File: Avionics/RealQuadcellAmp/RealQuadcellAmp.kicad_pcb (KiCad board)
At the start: 2 copper layers, 115 x 90.5 mm, 73 parts, among them J1 Screw_Terminal_01x02, J2 Conn_01x04_Pin, U1 OPA1642AID, U2 OPA1642AID, U3 OPA1642AID, U4 OPA1642AID

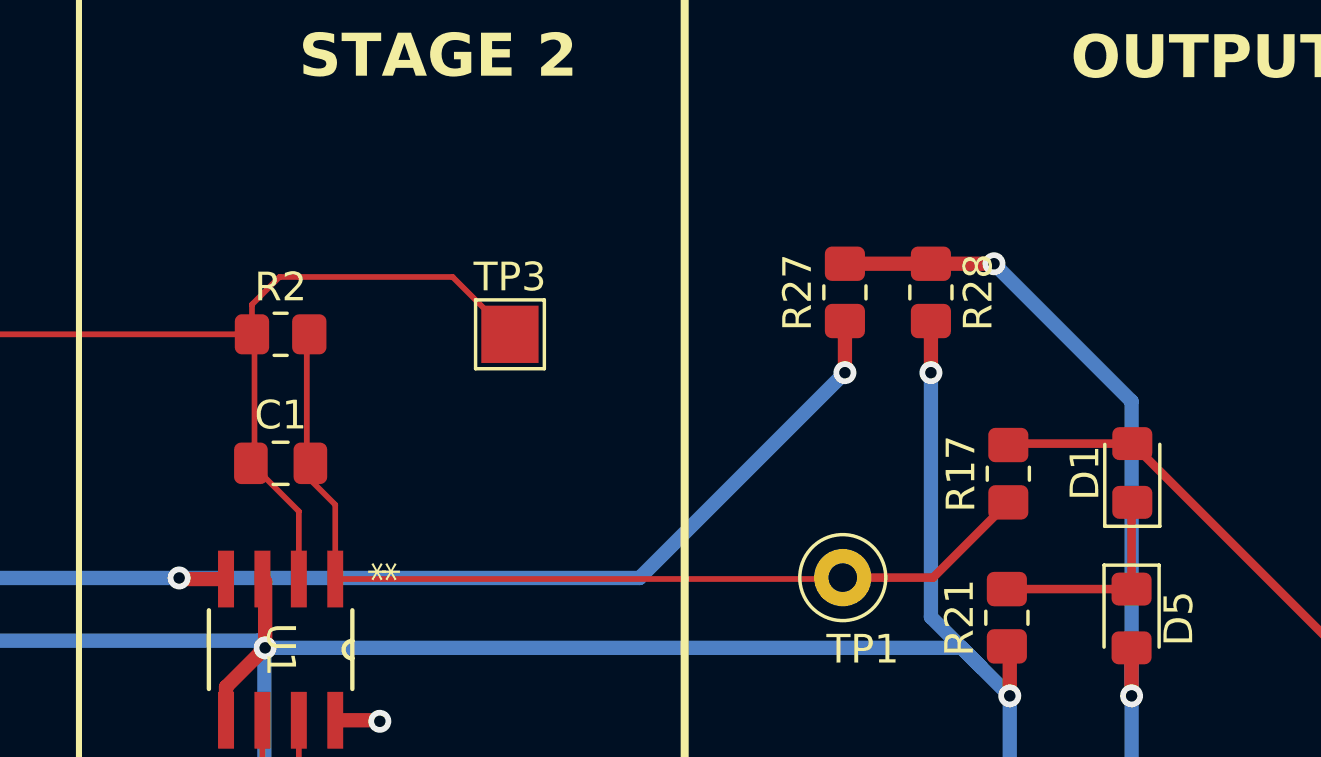
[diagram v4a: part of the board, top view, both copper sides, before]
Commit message: added voltage regulator
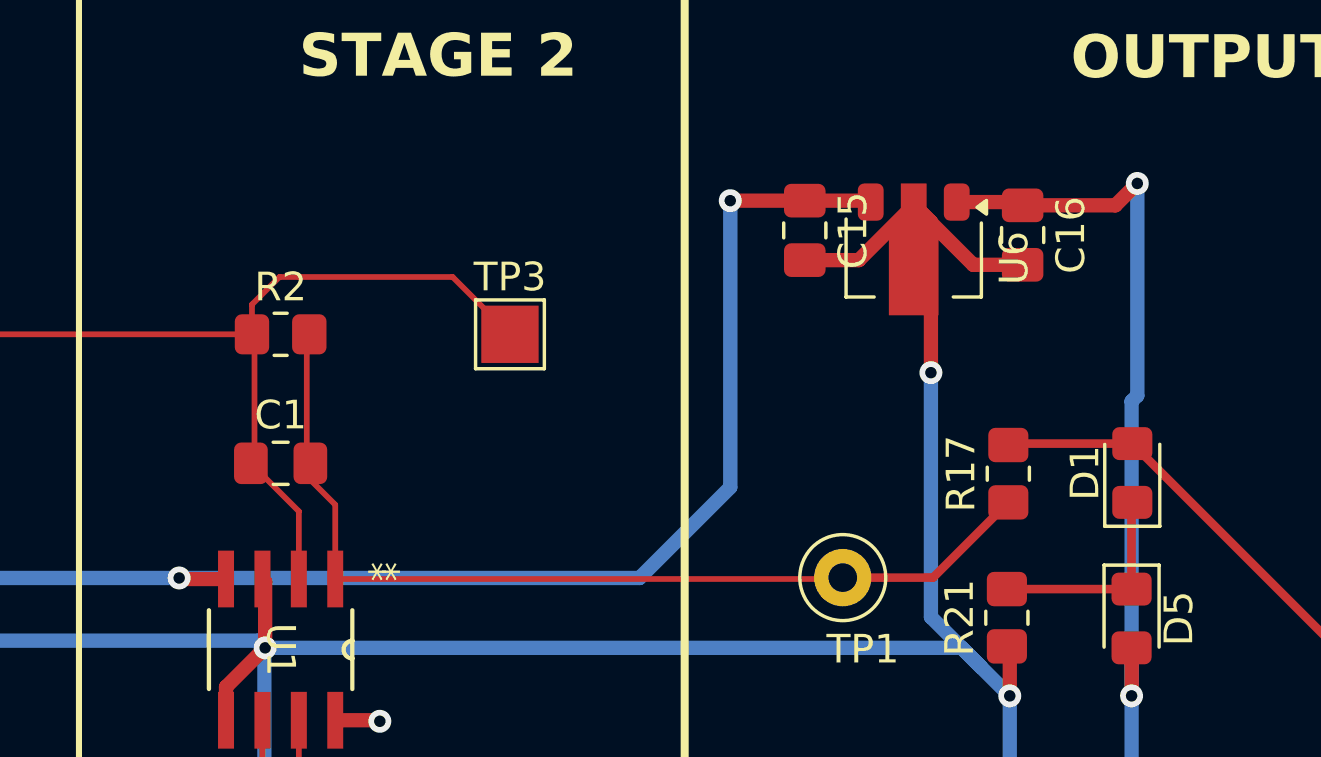
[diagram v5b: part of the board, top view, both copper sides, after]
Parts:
- removed R27: 11k, Resistor_SMD:R_0805_2012Metric_Pad1.20x1.40mm_HandSolder
- removed R28: 29k, Resistor_SMD:R_0805_2012Metric_Pad1.20x1.40mm_HandSolder
- added C15: 0.33u, Capacitor_SMD:C_0805_2012Metric_Pad1.18x1.45mm_HandSolder, F.Cu at (171.6, 49.4)
- added C16: 0.1u, Capacitor_SMD:C_0805_2012Metric_Pad1.18x1.45mm_HandSolder, F.Cu at (179.2, 49.6)
- added U6: L78L33_SOT89, Package_TO_SOT_SMD:SOT-89-3, F.Cu at (175.4, 50.4)
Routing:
- net QUAD_GND: track 308.6 -> 322.2 mm
- net VCC: track 181.0 -> 188.5 mm
- net +3V3: track 75.9 -> 78.2 mm

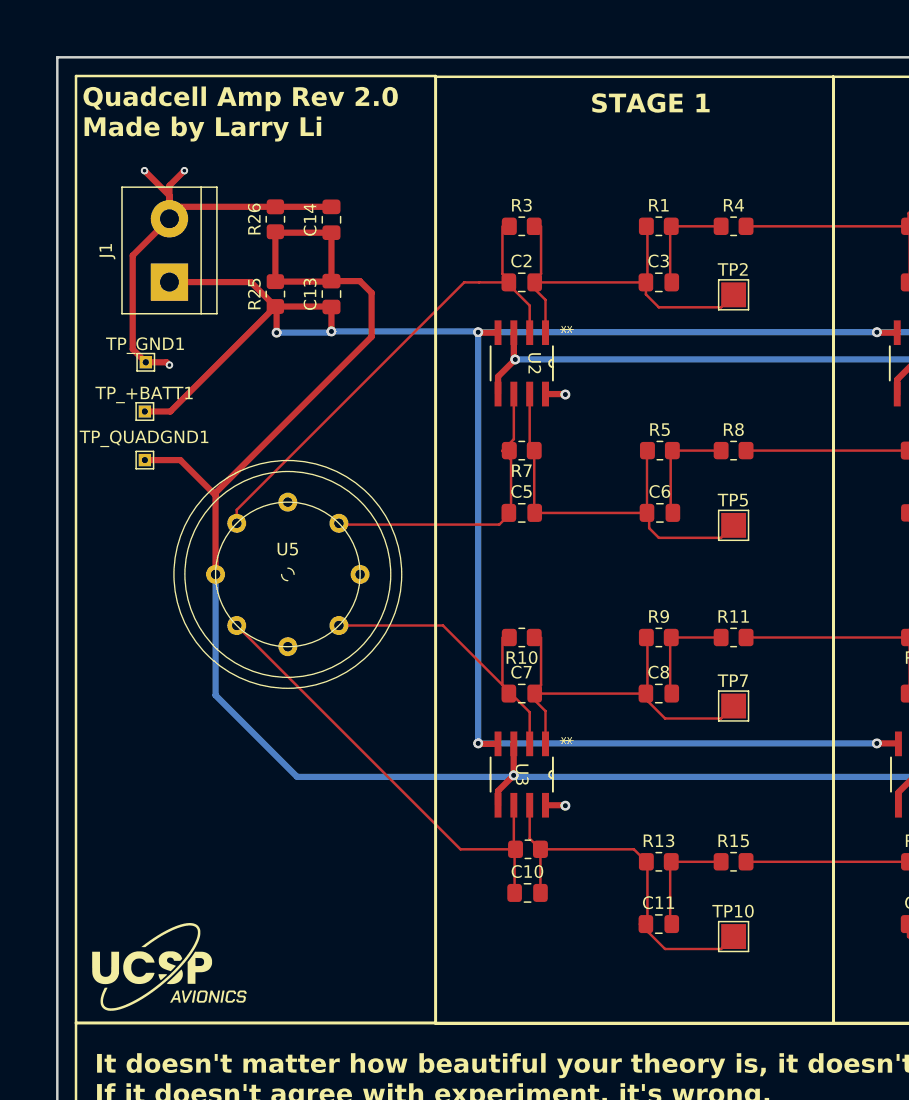
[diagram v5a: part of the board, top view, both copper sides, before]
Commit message: aesthetic changes + added zumi's name
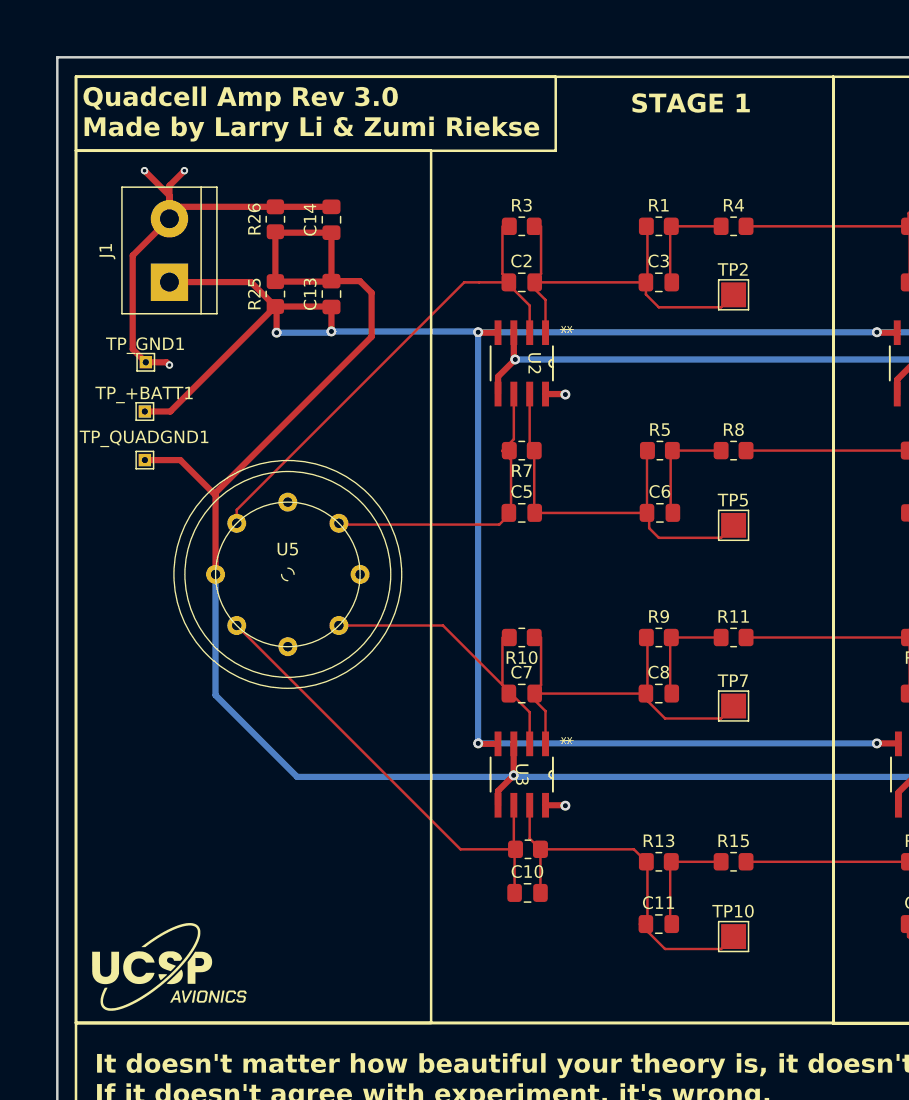
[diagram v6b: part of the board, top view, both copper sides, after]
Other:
- board text added: "Quadcell Amp Rev 3.0 Made by Larry Li & Zumi Riekse"
- board text removed: "Quadcell Amp Rev 2.0 Made by Larry Li"
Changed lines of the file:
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@@
 		)
 		(fp_text user "${REFERENCE}"
-			(at 0.2 0 360)
+			(at 0.2 0 0)
 			(layer "F.Fab")
 			(effects
@@
 			)
 		)
-		(property "Footprint" "UCSP_avionics_logo"
+		(property "Footprint" "UCSP:UCSP_avionics_logo"
 			(at 0 0 0)
 			(unlocked yes)
@@
 	)
 	(gr_rect
-		(start 146.275 41.0625)
-		(end 167.45 117.0625)
+		(start 85.5 41.0625)
+		(end 124 47)
+		(stroke
+			(width 0.2)
+			(type default)
+		)
+		(fill none)
+		(layer "F.SilkS")
+	)
+	(gr_rect
+		(start 85.5 47)
+		(end 114 117)
 		(stroke
 			(width 0.2)
@@
 	)
 	(gr_rect
-		(start 85.5 41)
-		(end 114.375 117)
+		(start 146.275 41.0625)
+		(end 167.45 117.0625)
 		(stroke
 			(width 0.2)
@@
 	)
 	(gr_rect
-		(start 114.375 41.0625)
-		(end 146.275 117.0625)
+		(start 85.5 41.0625)
+		(end 146.275 117)
 		(stroke
 			(width 0.2)
@@
 	)
 	(gr_text "STAGE 1"
-		(at 126.775 44.1 0)
+		(at 130 44.1 0)
 		(layer "F.SilkS")
 		(effects
@@
 		)
 	)
-	(gr_text "Quadcell Amp Rev 2.0\nMade by Larry Li"
+	(gr_text "Quadcell Amp Rev 3.0\nMade by Larry Li & Zumi Riekse"
 		(at 86 46 0)
 		(layer "F.SilkS")

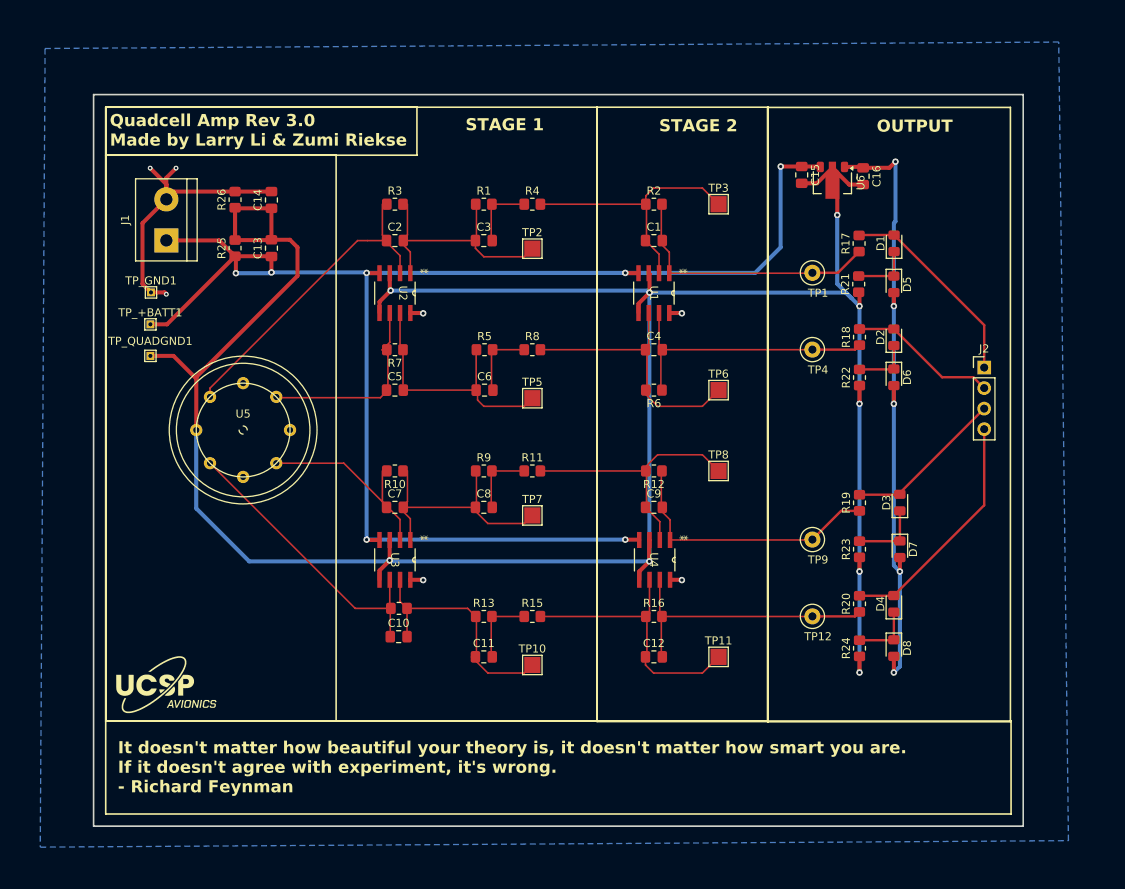
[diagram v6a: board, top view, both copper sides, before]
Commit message: changed gnd plane
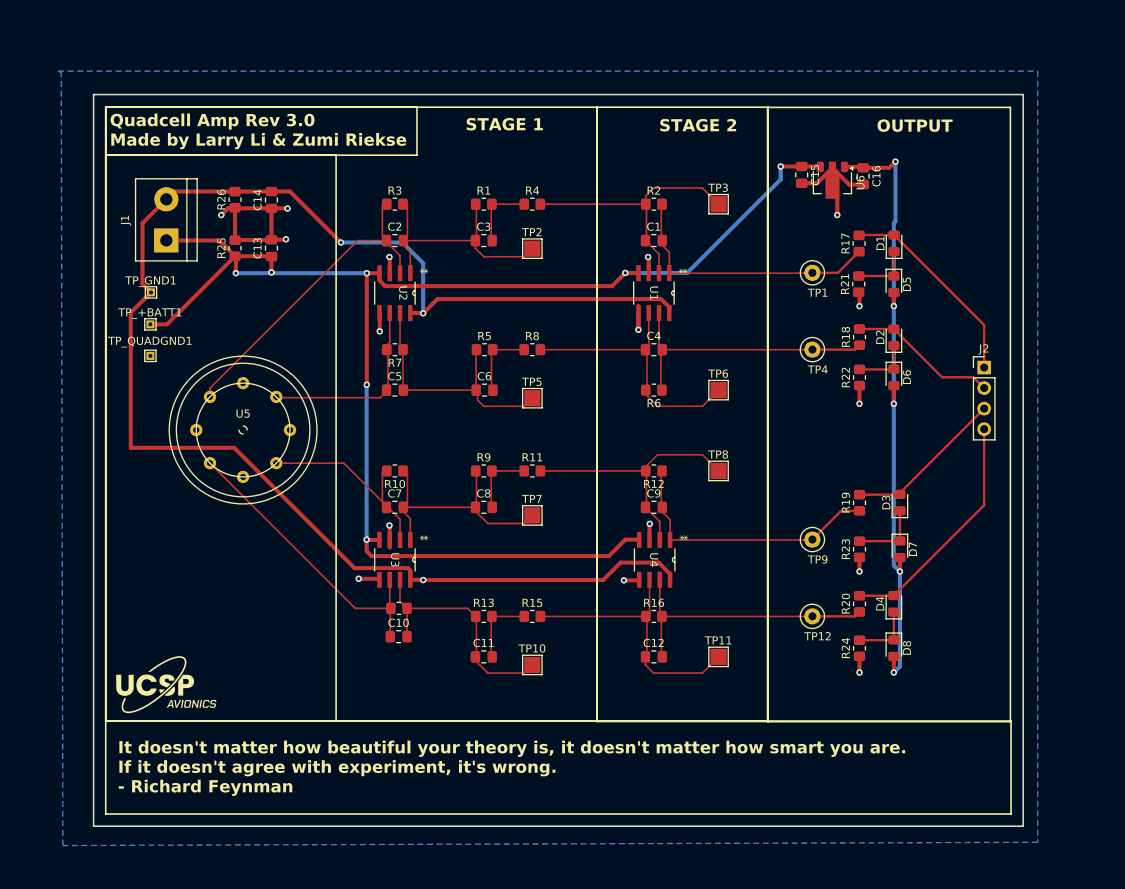
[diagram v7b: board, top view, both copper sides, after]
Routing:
- net QUAD_GND: track 322.2 -> 71.3 mm, vias 9 -> 16
- net GND: track 44.1 -> 185.9 mm, vias 7 -> 3
- net VCC: track 188.5 -> 186.5 mm
- added copper zone on B.Cu, net QUAD_GND
- removed copper zone on B.Cu, net GND

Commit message: added intermediary connectors and voltage caps after stage 1
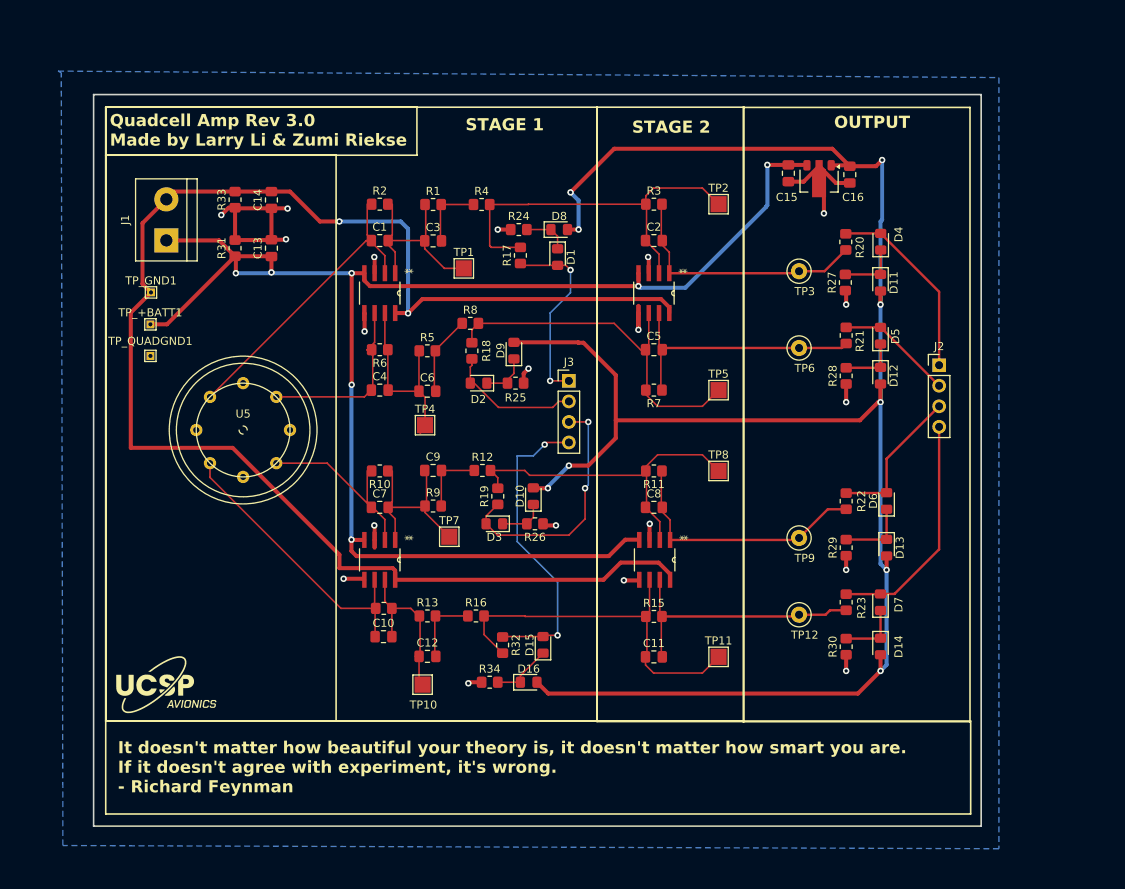
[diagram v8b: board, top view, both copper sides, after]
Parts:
- added D1: ~, Diode_SMD:D_0805_2012Metric_Pad1.15x1.40mm_HandSolder, F.Cu at (141.4, 59.6)
- added D10: ~, Diode_SMD:D_0805_2012Metric_Pad1.15x1.40mm_HandSolder, F.Cu at (138.4, 89.2)
- added D15: ~, Diode_SMD:D_0805_2012Metric_Pad1.15x1.40mm_HandSolder, F.Cu at (139.6, 107.6)
- added D16: ~, Diode_SMD:D_0805_2012Metric_Pad1.15x1.40mm_HandSolder, F.Cu at (137.8, 112.2)
- added D2: ~, Diode_SMD:D_0805_2012Metric_Pad1.15x1.40mm_HandSolder, F.Cu at (131.6, 75.2)
- added D3: ~, Diode_SMD:D_0805_2012Metric_Pad1.15x1.40mm_HandSolder, F.Cu at (133.6, 92.6)
- added D8: ~, Diode_SMD:D_0805_2012Metric_Pad1.15x1.40mm_HandSolder, F.Cu at (141.6, 56.2)
- added D9: ~, Diode_SMD:D_0805_2012Metric_Pad1.15x1.40mm_HandSolder, F.Cu at (136.0, 71.2)
- added J3: Conn_01x04_Pin, Connector_PinHeader_2.54mm:PinHeader_1x04_P2.54mm_Vertical, F.Cu at (142.8, 74.9)
- added R17: 1 kΩ, Resistor_SMD:R_0805_2012Metric_Pad1.20x1.40mm_HandSolder, F.Cu at (136.8, 59.4)
- added R18: 1 kΩ, Resistor_SMD:R_0805_2012Metric_Pad1.20x1.40mm_HandSolder, F.Cu at (130.8, 71.2)
- added R19: 1 kΩ, Resistor_SMD:R_0805_2012Metric_Pad1.20x1.40mm_HandSolder, F.Cu at (134.0, 89.2)
- added R24: 40 Ω, Resistor_SMD:R_0805_2012Metric_Pad1.20x1.40mm_HandSolder, F.Cu at (136.6, 56.2)
- added R25: 40 Ω, Resistor_SMD:R_0805_2012Metric_Pad1.20x1.40mm_HandSolder, F.Cu at (136.2, 75.2)
- added R26: 40 Ω, Resistor_SMD:R_0805_2012Metric_Pad1.20x1.40mm_HandSolder, F.Cu at (138.6, 92.6)
- added R32: 1 kΩ, Resistor_SMD:R_0805_2012Metric_Pad1.20x1.40mm_HandSolder, F.Cu at (134.6, 107.6)
- added R34: 40 Ω, Resistor_SMD:R_0805_2012Metric_Pad1.20x1.40mm_HandSolder, F.Cu at (133.0, 112.2)
- R1: value 68.1 kΩ -> 68.1k
- moved TP10 13.8 mm to (124.7, 112.5)
- moved TP4 13.7 mm to (125.0, 80.4)
- moved TP7 10.6 mm to (128.0, 94.2)
- moved TP1 8.82 mm to (129.8, 61.0)
- moved R8 8.34 mm to (130.6, 67.8)
- moved C9 7.76 mm to (126.0, 86.0)
- moved R9 7.63 mm to (126.0, 90.4)
- moved C6 7.08 mm to (125.3, 76.2)
- moved R5 7.08 mm to (125.3, 71.2)
- moved C12 6.98 mm to (125.3, 109.0)
- moved R13 6.98 mm to (125.3, 104.0)
- moved R16 6.98 mm to (131.3, 104.0)
- moved C3 6.28 mm to (126.0, 57.6)
- moved R1 6.28 mm to (126.0, 53.1)
- moved R4 6.28 mm to (132.0, 53.1)
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- renumbered C2 to C1, C12 to C11, C11 to C12, C1 to C2, C5 to C4, C4 to C5, C9 to C8, C8 to C9, D5 to D11, D6 to D12, D7 to D13, D8 to D14, D1 to D4, D2 to D5, D3 to D6, D4 to D7, R12 to R11, R11 to R12, R16 to R15, R15 to R16, R3 to R2, R17 to R20, R18 to R21, R19 to R22, R20 to R23, R21 to R27, R22 to R28, R23 to R29, R2 to R3, R24 to R30, R25 to R31, R26 to R33, R7 to R6, R6 to R7, TP2 to TP1, TP3 to TP2, TP1 to TP3, TP5 to TP4, TP6 to TP5, TP4 to TP6, U2 to U1, U1 to U2
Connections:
- R20 pad 1: /STAGE2_OUT1 -> /FOUT1
- R20 pad 2: /FOUT1 -> /STAGE2_OUT1
- R21 pad 1: /STAGE2_OUT2 -> /FOUT2
- R21 pad 2: /FOUT2 -> /STAGE2_OUT2
- R22 pad 1: /STAGE2_OUT3 -> /FOUT3
- R22 pad 2: /FOUT3 -> /STAGE2_OUT3
- R23 pad 1: /STAGE2_OUT4 -> /FOUT4
- R23 pad 2: /FOUT4 -> /STAGE2_OUT4
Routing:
- net +3V3: track 78.2 -> 235.2 mm, vias 5 -> 9
- net /MOUT4: track 0.00 -> 38.2 mm, vias 0 -> 2
- net /MOUT3: track 0.00 -> 31.2 mm, vias 0 -> 2
- net /MOUT1: track 0.00 -> 23.6 mm, vias 0 -> 2
- net /MOUT2: track 0.00 -> 16.8 mm
- net /STAGE1_OUT1: track 33.7 -> 48.8 mm
- net /STAGE1_OUT4: track 34.2 -> 46.7 mm
- net /STAGE1_OUT2: track 33.9 -> 45.4 mm
- net Net-(U3-OUTB): track 30.3 -> 20.4 mm
- net /STAGE1_OUT3: track 33.4 -> 41.8 mm
- net Net-(U3-OUTA): track 31.5 -> 23.5 mm
- net Net-(U1-OUTB): track 32.5 -> 24.5 mm
- net Net-(D15-K): track 0.00 -> 7.56 mm
- net QUAD_GND: track 71.3 -> 78.4 mm, vias 16 -> 20
- net Net-(U1-OUTA): track 31.9 -> 25.1 mm
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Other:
- board size 115 x 90.5 mm -> 109.8 x 90.5 mm
